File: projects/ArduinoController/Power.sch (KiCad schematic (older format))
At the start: 20 parts

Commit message: working on schematics of Arduino Controller
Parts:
- added U?: ISL21070, symbol ISL21070
- D?: value LED -> V_BAT
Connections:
- net GND: now also U?.3 (GND)
- net VCC_3V3: now also U?.1 (IN)
- new net 2V_Vcc: U?.2 (OUT)
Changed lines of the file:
@@
 	1    0    0    -1
 $EndComp
-Text GLabel 8550 3100 1    47   Output ~ 0
+Text GLabel 8550 3300 1    47   Output ~ 0
 VCC_3V3
 $Comp
@@
 	2700 3800 2700 4250
 Wire Wire Line
-	5000 2750 7900 2750
+	5000 2750 9900 2750
 Connection ~ 5600 2750
 Wire Wire Line
@@
 Wire Wire Line
 	5000 2750 5000 3100
-Text HLabel 7900 2750 2    47   Output ~ 0
+Text HLabel 9900 2750 2    47   Output ~ 0
 5V_Vcc
-Text HLabel 8700 3750 2    47   Output ~ 0
+Text HLabel 9900 3250 2    47   Output ~ 0
 3V3_Vcc
 Connection ~ 7750 2750
@@
 Wire Wire Line
 	7750 3750 7750 2750
-Wire Wire Line
-	8550 3750 8550 3100
 $Comp
 L SWITCH-SPSTPTH2 S?
@@
 P 3250 5250
 F 0 "D?" H 3100 5350 50  0000 C CNN
-F 1 "LED" H 3325 5350 50  0000 C CNN
+F 1 "V_BAT" H 3325 5350 50  0000 C CNN
 F 2 "" H 3250 5250 60  0000 C CNN
 F 3 "" H 3250 5250 60  0000 C CNN
@@
 $EndComp
 Connection ~ 3250 4550
+$Comp
+L ISL21070 U?
+U 1 1 556B667E
+P 9225 3825
+F 0 "U?" H 9225 4125 60  0000 C CNN
+F 1 "ISL21070" H 9225 4025 60  0000 C CNN
+F 2 "" H 9225 3725 60  0000 C CNN
+F 3 "" H 9225 3725 60  0000 C CNN
+	1    9225 3825
+	1    0    0    -1
+$EndComp
+Text HLabel 9900 3750 2    47   Output ~ 0
+2V_Vcc
+$Comp
+L GND #PWR?
+U 1 1 556B66A2
+P 9225 4300
+F 0 "#PWR?" H 9225 4300 30  0001 C CNN
+F 1 "GND" H 9225 4230 30  0001 C CNN
+F 2 "" H 9225 4300 60  0000 C CNN
+F 3 "" H 9225 4300 60  0000 C CNN
+	1    9225 4300
+	1    0    0    -1
+$EndComp
+Wire Wire Line
+	8550 3750 8550 3300
+Wire Wire Line
+	9900 3250 8700 3250
+Wire Wire Line
+	8700 3250 8700 3750
+Wire Wire Line
+	9900 3750 9750 3750
 $EndSCHEMATC

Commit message: work in progress
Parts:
- R?: value R -> 220
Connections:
- net GND: now also S?.1 (O)
- net V_BATT: no longer R?.1
- net Batt_5V: now reaches C?.1, Q?.3 (D), U?.2 (VO)
- net Batt_5V: now also R?.1
- no-connect marks 2 -> 1
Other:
- note added: "Dual OpAmp:\nz.B. LM358\n(SOIC-8)"
- moved on the sheet: D?, R?
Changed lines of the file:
@@
 Wire Wire Line
 	2850 4450 2700 4450
-NoConn ~ 2850 4650
 Wire Wire Line
 	3150 4550 3450 4550
@@
 L R R?
 U 1 1 556AF6F0
-P 3250 4800
-F 0 "R?" V 3330 4800 40  0000 C CNN
-F 1 "R" V 3257 4801 40  0000 C CNN
-F 2 "" V 3180 4800 30  0000 C CNN
-F 3 "" H 3250 4800 30  0000 C CNN
-	1    3250 4800
-	1    0    0    -1
+P 2050 5200
+F 0 "R?" V 2130 5200 40  0000 C CNN
+F 1 "220" V 2057 5201 40  0000 C CNN
+F 2 "" V 1980 5200 30  0000 C CNN
+F 3 "" H 2050 5200 30  0000 C CNN
+	1    2050 5200
+	0    -1   -1   0
 $EndComp
 $Comp
 L LED D?
 U 1 1 556AF704
-P 3250 5250
-F 0 "D?" H 3100 5350 50  0000 C CNN
-F 1 "V_BAT" H 3325 5350 50  0000 C CNN
-F 2 "" H 3250 5250 60  0000 C CNN
-F 3 "" H 3250 5250 60  0000 C CNN
-	1    3250 5250
-	0    1    1    0
+P 2500 5200
+F 0 "D?" H 2350 5300 50  0000 C CNN
+F 1 "V_BAT" H 2575 5300 50  0000 C CNN
+F 2 "" H 2500 5200 60  0000 C CNN
+F 3 "" H 2500 5200 60  0000 C CNN
+	1    2500 5200
+	1    0    0    -1
 $EndComp
 $Comp
 L GND #PWR?
 U 1 1 556AF716
-P 3250 5450
-F 0 "#PWR?" H 3250 5450 30  0001 C CNN
-F 1 "GND" H 3250 5380 30  0001 C CNN
-F 2 "" H 3250 5450 60  0000 C CNN
-F 3 "" H 3250 5450 60  0000 C CNN
-	1    3250 5450
-	1    0    0    -1
+P 2700 5200
+F 0 "#PWR?" H 2700 5200 30  0001 C CNN
+F 1 "GND" H 2700 5130 30  0001 C CNN
+F 2 "" H 2700 5200 60  0000 C CNN
+F 3 "" H 2700 5200 60  0000 C CNN
+	1    2700 5200
+	0    -1   -1   0
 $EndComp
 Connection ~ 3250 4550
@@
 Wire Wire Line
 	9900 3750 9750 3750
+$Comp
+L GND #PWR?
+U 1 1 556CA095
+P 2850 4650
+F 0 "#PWR?" H 2850 4650 30  0001 C CNN
+F 1 "GND" H 2850 4580 30  0001 C CNN
+F 2 "" H 2850 4650 60  0000 C CNN
+F 3 "" H 2850 4650 60  0000 C CNN
+	1    2850 4650
+	0    1    1    0
+$EndComp
+Text GLabel 6300 4200 0    47   Output ~ 0
+Batt_5V
+Wire Wire Line
+	6550 3750 6550 4200
+Wire Wire Line
+	6550 4200 6300 4200
+Text GLabel 1800 5200 0    47   Input ~ 0
+Batt_5V
+Text Notes 4575 4975 0    60   ~ 0
+Dual OpAmp:\nz.B. LM358\n(SOIC-8)
 $EndSCHEMATC

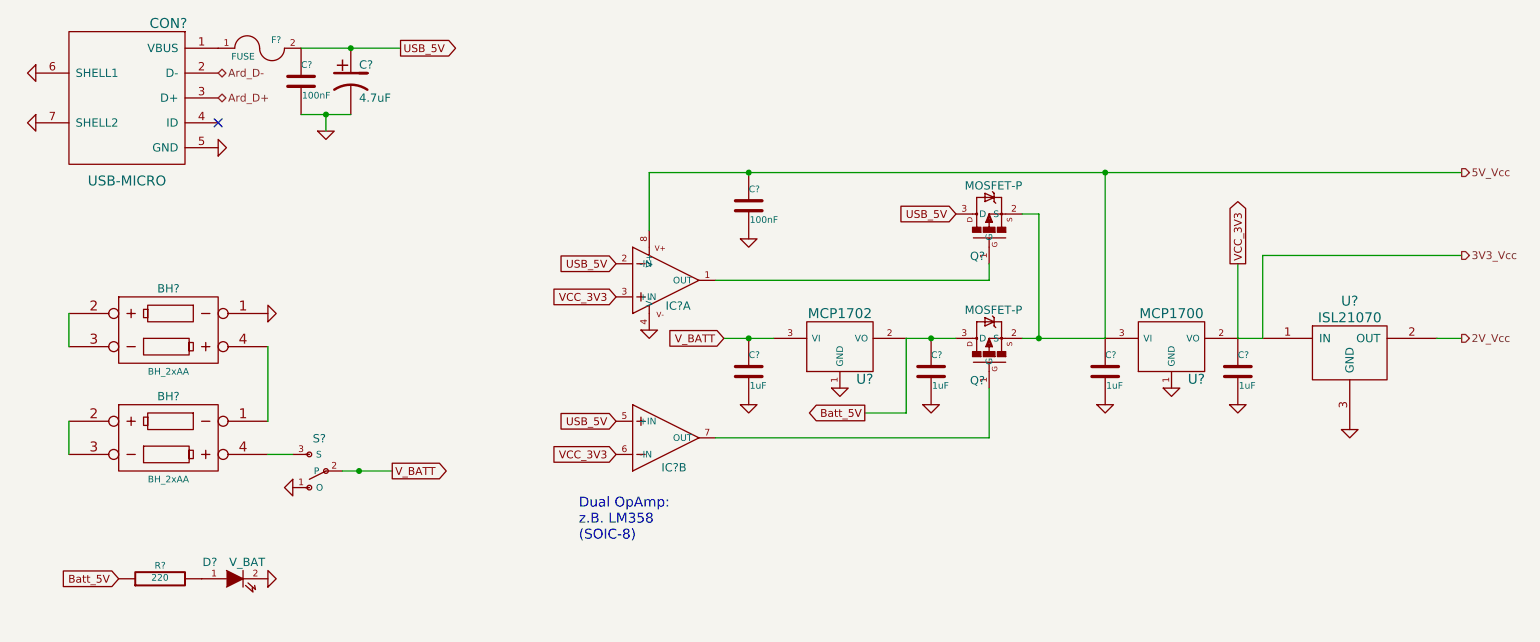
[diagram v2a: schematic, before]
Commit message: schematic passes ERC
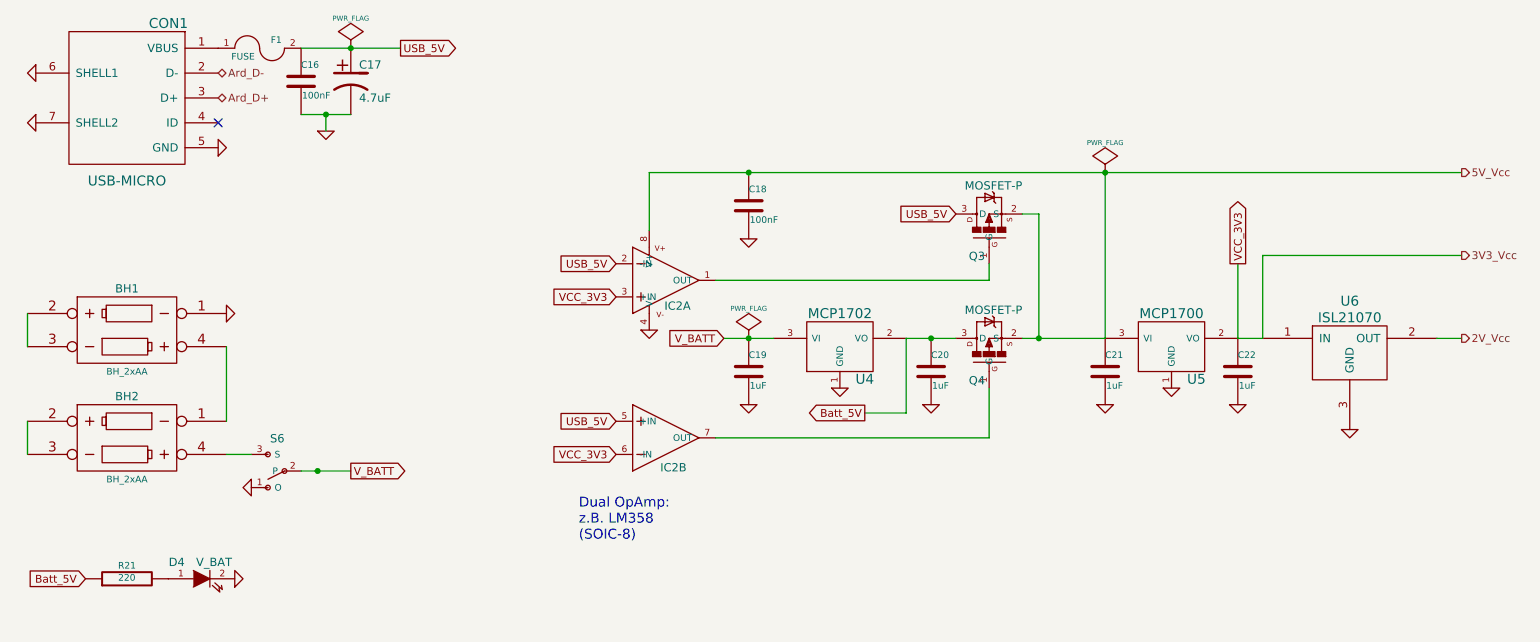
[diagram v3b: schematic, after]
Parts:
- removed BH? (x2): BH_2xAA, symbol BH_2xAA
- removed U?: MCP1702, symbol MCP1702
- removed U?: ISL21070, symbol ISL21070
- added BH1, BH2: BH_2xAA, symbol BH_2xAA
- added U4: MCP1702, symbol MCP1702
- added U6: ISL21070, symbol ISL21070
- gave numbers to parts that had none: 16
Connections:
- net 2V_Vcc: now also U6.2 (OUT)
- net Batt_5V: now also U4.2 (VO)
- net GND: now also BH1.1, U4.1 (GND), U6.3 (GND)
- net VCC_3V3: now also U6.1 (IN)
- net V_BATT: now also U4.3 (VI)
- net at S6.3 (S): now also BH2.4
- new net: BH1.2, BH1.3
- new net: BH1.4, BH2.1
- new net: BH2.2, BH2.3
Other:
- moved on the sheet: D4, R21, S6

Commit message: working on footprints and netlist
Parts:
- removed U4: MCP1702, symbol MCP1702
- added CN1: DCBARREL, DCJACK, symbol DCBARREL
- added U4: NCP1117, symbol NCP1117
- C22: renamed from C19; value 1uF -> 10uF
- C23: renamed from C20; value 1uF -> 10uF
- IC2: value OPAMP-DUALU -> OPAMP-LM358
- renumbered C16 to C19, C17 to C20, C18 to C21, C21 to C24, C22 to C25
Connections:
- net Batt_5V: now also IC2.2 (-IN), IC2.5 (+IN), U4.2 (VO)
- net GND: now also CN1.GND, CN1.GNDB (GNDBREAK), U4.1 (GND); no longer S6.1 (O)
- net USB_5V: no longer IC2.2 (-IN), IC2.5 (+IN)
- net V_BATT: now also U4.3 (VI)
- new net: CN1.PWR, S6.1 (O)
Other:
- note removed: "Dual OpAmp:\nz.B. LM358\n(SOIC-8)"
- moved on the sheet: D4, R21
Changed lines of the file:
@@
 USB_5V
 $Comp
-L GND #PWR053
+L GND #PWR052
 U 1 1 5569964F
 P 2400 2600
-F 0 "#PWR053" H 2400 2600 30  0001 C CNN
+F 0 "#PWR052" H 2400 2600 30  0001 C CNN
 F 1 "GND" H 2400 2530 30  0001 C CNN
 F 2 "" H 2400 2600 60  0000 C CNN
@@
 $EndComp
 $Comp
-L GND #PWR054
+L GND #PWR053
 U 1 1 55699661
 P 1300 2150
-F 0 "#PWR054" H 1300 2150 30  0001 C CNN
+F 0 "#PWR053" H 1300 2150 30  0001 C CNN
 F 1 "GND" H 1300 2080 30  0001 C CNN
 F 2 "" H 1300 2150 60  0000 C CNN
@@
 $EndComp
 $Comp
-L GND #PWR055
+L GND #PWR054
 U 1 1 5569966C
 P 1300 2450
-F 0 "#PWR055" H 1300 2450 30  0001 C CNN
+F 0 "#PWR054" H 1300 2450 30  0001 C CNN
 F 1 "GND" H 1300 2380 30  0001 C CNN
 F 2 "" H 1300 2450 60  0000 C CNN
@@
 $EndComp
 $Comp
-L C C16
+L C C19
 U 1 1 55699766
 P 2900 2200
-F 0 "C16" H 2900 2300 40  0000 L CNN
+F 0 "C19" H 2900 2300 40  0000 L CNN
 F 1 "100nF" H 2906 2115 40  0000 L CNN
 F 2 "" H 2938 2050 30  0000 C CNN
@@
 $EndComp
 $Comp
-L CP1 C17
+L CP1 C20
 U 1 1 5569977A
 P 3200 2200
-F 0 "C17" H 3250 2300 50  0000 L CNN
+F 0 "C20" H 3250 2300 50  0000 L CNN
 F 1 "4.7uF" H 3250 2100 50  0000 L CNN
 F 2 "" H 3200 2200 60  0000 C CNN
@@
 $EndComp
 $Comp
-L GND #PWR056
+L GND #PWR055
 U 1 1 5569978E
 P 3050 2500
-F 0 "#PWR056" H 3050 2500 30  0001 C CNN
+F 0 "#PWR055" H 3050 2500 30  0001 C CNN
 F 1 "GND" H 3050 2430 30  0001 C CNN
 F 2 "" H 3050 2500 60  0000 C CNN
@@
 $EndComp
 $Comp
-L GND #PWR057
+L GND #PWR056
 U 1 1 5569BB18
 P 2450 3600
-F 0 "#PWR057" H 2450 3600 30  0001 C CNN
+F 0 "#PWR056" H 2450 3600 30  0001 C CNN
 F 1 "GND" H 2450 3530 30  0001 C CNN
 F 2 "" H 2450 3600 60  0000 C CNN
@@
 P 5100 4350
 F 0 "IC2" H 5225 4200 50  0000 R TNN
-F 1 "OPAMP-DUALU" H 5300 4550 50  0001 R TNN
+F 1 "OPAMP-LM358" H 5200 4775 50  0000 R TNN
 F 2 "SparkFun-SO08" H 5100 4500 50  0001 C CNN
 F 3 "" H 5100 4350 60  0000 C CNN
@@
 VCC_3V3
 $Comp
-L C C20
+L C C23
 U 1 1 5569F285
 P 6700 3950
-F 0 "C20" H 6700 4050 40  0000 L CNN
-F 1 "1uF" H 6706 3865 40  0000 L CNN
+F 0 "C23" H 6700 4050 40  0000 L CNN
+F 1 "10uF" H 6706 3865 40  0000 L CNN
 F 2 "" H 6738 3800 30  0000 C CNN
 F 3 "" H 6700 3950 60  0000 C CNN
@@
 $EndComp
 $Comp
-L C C19
+L C C22
 U 1 1 5569F290
 P 5600 3950
-F 0 "C19" H 5600 4050 40  0000 L CNN
-F 1 "1uF" H 5606 3865 40  0000 L CNN
+F 0 "C22" H 5600 4050 40  0000 L CNN
+F 1 "10uF" H 5606 3865 40  0000 L CNN
 F 2 "" H 5638 3800 30  0000 C CNN
 F 3 "" H 5600 3950 60  0000 C CNN
@@
 $EndComp
 $Comp
-L GND #PWR058
+L GND #PWR057
 U 1 1 5569F41E
 P 5600 4150
-F 0 "#PWR058" H 5600 4150 30  0001 C CNN
+F 0 "#PWR057" H 5600 4150 30  0001 C CNN
 F 1 "GND" H 5600 4080 30  0001 C CNN
 F 2 "" H 5600 4150 60  0000 C CNN
@@
 $EndComp
 $Comp
-L GND #PWR059
+L GND #PWR058
 U 1 1 5569F429
 P 6700 4150
-F 0 "#PWR059" H 6700 4150 30  0001 C CNN
+F 0 "#PWR058" H 6700 4150 30  0001 C CNN
 F 1 "GND" H 6700 4080 30  0001 C CNN
 F 2 "" H 6700 4150 60  0000 C CNN
@@
 $EndComp
 $Comp
-L GND #PWR060
+L GND #PWR059
 U 1 1 5569F452
 P 6150 4050
-F 0 "#PWR060" H 6150 4050 30  0001 C CNN
+F 0 "#PWR059" H 6150 4050 30  0001 C CNN
 F 1 "GND" H 6150 3980 30  0001 C CNN
 F 2 "" H 6150 4050 60  0000 C CNN
@@
 $EndComp
 $Comp
-L GND #PWR061
+L GND #PWR060
 U 1 1 5569F467
 P 5000 3700
-F 0 "#PWR061" H 5000 3700 30  0001 C CNN
+F 0 "#PWR060" H 5000 3700 30  0001 C CNN
 F 1 "GND" H 5000 3630 30  0001 C CNN
 F 2 "" H 5000 3700 60  0000 C CNN
@@
 $EndComp
 $Comp
-L C C18
+L C C21
 U 1 1 5569F472
 P 5600 2950
-F 0 "C18" H 5600 3050 40  0000 L CNN
+F 0 "C21" H 5600 3050 40  0000 L CNN
 F 1 "100nF" H 5606 2865 40  0000 L CNN
 F 2 "" H 5638 2800 30  0000 C CNN
@@
 $EndComp
 $Comp
-L GND #PWR062
+L GND #PWR061
 U 1 1 5569F482
 P 5600 3150
-F 0 "#PWR062" H 5600 3150 30  0001 C CNN
+F 0 "#PWR061" H 5600 3150 30  0001 C CNN
 F 1 "GND" H 5600 3080 30  0001 C CNN
 F 2 "" H 5600 3150 60  0000 C CNN
@@
 VCC_3V3
 Text GLabel 4800 3300 0    47   Input ~ 0
-USB_5V
+Batt_5V
 Text GLabel 4800 4250 0    47   Input ~ 0
-USB_5V
-$Comp
-L C C21
+Batt_5V
+$Comp
+L C C24
 U 1 1 5569FAC7
 P 7750 3950
-F 0 "C21" H 7750 4050 40  0000 L CNN
+F 0 "C24" H 7750 4050 40  0000 L CNN
 F 1 "1uF" H 7756 3865 40  0000 L CNN
 F 2 "" H 7788 3800 30  0000 C CNN
@@
 $EndComp
 $Comp
-L C C22
+L C C25
 U 1 1 5569FAD2
 P 8550 3950
-F 0 "C22" H 8550 4050 40  0000 L CNN
+F 0 "C25" H 8550 4050 40  0000 L CNN
 F 1 "1uF" H 8556 3865 40  0000 L CNN
 F 2 "" H 8588 3800 30  0000 C CNN
@@
 $EndComp
 $Comp
-L GND #PWR063
+L GND #PWR062
 U 1 1 5569FB9D
 P 7750 4150
-F 0 "#PWR063" H 7750 4150 30  0001 C CNN
+F 0 "#PWR062" H 7750 4150 30  0001 C CNN
 F 1 "GND" H 7750 4080 30  0001 C CNN
 F 2 "" H 7750 4150 60  0000 C CNN
@@
 $EndComp
 $Comp
-L GND #PWR064
+L GND #PWR063
 U 1 1 5569FBA8
 P 8150 4050
-F 0 "#PWR064" H 8150 4050 30  0001 C CNN
+F 0 "#PWR063" H 8150 4050 30  0001 C CNN
 F 1 "GND" H 8150 3980 30  0001 C CNN
 F 2 "" H 8150 4050 60  0000 C CNN
@@
 $EndComp
 $Comp
-L GND #PWR065
+L GND #PWR064
 U 1 1 5569FBB3
 P 8550 4150
-F 0 "#PWR065" H 8550 4150 30  0001 C CNN
+F 0 "#PWR064" H 8550 4150 30  0001 C CNN
 F 1 "GND" H 8550 4080 30  0001 C CNN
 F 2 "" H 8550 4150 60  0000 C CNN
@@
 L R R21
 U 1 1 556AF6F0
-P 1850 5200
-F 0 "R21" V 1930 5200 40  0000 C CNN
-F 1 "220" V 1857 5201 40  0000 C CNN
-F 2 "" V 1780 5200 30  0000 C CNN
-F 3 "" H 1850 5200 30  0000 C CNN
-	1    1850 5200
+P 6400 4900
+F 0 "R21" V 6480 4900 40  0000 C CNN
+F 1 "220" V 6407 4901 40  0000 C CNN
+F 2 "" V 6330 4900 30  0000 C CNN
+F 3 "" H 6400 4900 30  0000 C CNN
+	1    6400 4900
 	0    -1   -1   0
 $EndComp
@@
 L LED D4
 U 1 1 556AF704
-P 2300 5200
-F 0 "D4" H 2150 5300 50  0000 C CNN
-F 1 "V_BAT" H 2375 5300 50  0000 C CNN
-F 2 "" H 2300 5200 60  0000 C CNN
-F 3 "" H 2300 5200 60  0000 C CNN
-	1    2300 5200
-	1    0    0    -1
-$EndComp
-$Comp
-L GND #PWR066
+P 6850 4900
+F 0 "D4" H 6700 5000 50  0000 C CNN
+F 1 "V_BAT" H 6925 5000 50  0000 C CNN
+F 2 "" H 6850 4900 60  0000 C CNN
+F 3 "" H 6850 4900 60  0000 C CNN
+	1    6850 4900
+	1    0    0    -1
+$EndComp
+$Comp
+L GND #PWR065
 U 1 1 556AF716
-P 2500 5200
-F 0 "#PWR066" H 2500 5200 30  0001 C CNN
-F 1 "GND" H 2500 5130 30  0001 C CNN
-F 2 "" H 2500 5200 60  0000 C CNN
-F 3 "" H 2500 5200 60  0000 C CNN
-	1    2500 5200
+P 7050 4900
+F 0 "#PWR065" H 7050 4900 30  0001 C CNN
+F 1 "GND" H 7050 4830 30  0001 C CNN
+F 2 "" H 7050 4900 60  0000 C CNN
+F 3 "" H 7050 4900 60  0000 C CNN
+	1    7050 4900
 	0    -1   -1   0
 $EndComp
@@
 2V_Vcc
 $Comp
-L GND #PWR067
+L GND #PWR066
 U 1 1 556B66A2
 P 9225 4300
-F 0 "#PWR067" H 9225 4300 30  0001 C CNN
+F 0 "#PWR066" H 9225 4300 30  0001 C CNN
 F 1 "GND" H 9225 4230 30  0001 C CNN
 F 2 "" H 9225 4300 60  0000 C CNN
@@
 	9900 3750 9750 3750
 $Comp
-L GND #PWR068
+L GND #PWR067
 U 1 1 556CA095
-P 2600 4650
-F 0 "#PWR068" H 2600 4650 30  0001 C CNN
-F 1 "GND" H 2600 4580 30  0001 C CNN
-F 2 "" H 2600 4650 60  0000 C CNN
-F 3 "" H 2600 4650 60  0000 C CNN
-	1    2600 4650
-	0    1    1    0
+P 2600 5200
+F 0 "#PWR067" H 2600 5200 30  0001 C CNN
+F 1 "GND" H 2600 5130 30  0001 C CNN
+F 2 "" H 2600 5200 60  0000 C CNN
+F 3 "" H 2600 5200 60  0000 C CNN
+	1    2600 5200
+	1    0    0    -1
 $EndComp
 Text GLabel 6300 4200 0    47   Output ~ 0
@@
 Wire Wire Line
 	6550 4200 6300 4200
-Text GLabel 1600 5200 0    47   Input ~ 0
+Text GLabel 6150 4900 0    47   Input ~ 0
 Batt_5V
-Text Notes 4575 4975 0    60   ~ 0
-Dual OpAmp:\nz.B. LM358\n(SOIC-8)
-$Comp
-L MCP1702 U4
-U 1 1 556E9FC1
-P 6150 3800
-F 0 "U4" H 6300 3604 60  0000 C CNN
-F 1 "MCP1702" H 6150 4000 60  0000 C CNN
-F 2 "" H 6150 3800 60  0000 C CNN
-F 3 "" H 6150 3800 60  0000 C CNN
-	1    6150 3800
-	1    0    0    -1
-$EndComp
 $Comp
 L BH_2xAA BH1
@@
 $EndComp
 $Comp
-L PWR_FLAG #FLG069
+L PWR_FLAG #FLG068
 U 1 1 557177D7
 P 5600 3750
-F 0 "#FLG069" H 5600 3845 30  0001 C CNN
+F 0 "#FLG068" H 5600 3845 30  0001 C CNN
 F 1 "PWR_FLAG" H 5600 3930 30  0000 C CNN
 F 2 "" H 5600 3750 60  0000 C CNN
@@
 $EndComp
 $Comp
-L PWR_FLAG #FLG070
+L PWR_FLAG #FLG069
 U 1 1 55718314
 P 3200 2000
-F 0 "#FLG070" H 3200 2095 30  0001 C CNN
+F 0 "#FLG069" H 3200 2095 30  0001 C CNN
 F 1 "PWR_FLAG" H 3200 2180 30  0000 C CNN
 F 2 "" H 3200 2000 60  0000 C CNN
@@
 $EndComp
 $Comp
-L PWR_FLAG #FLG071
+L PWR_FLAG #FLG070
 U 1 1 557185B0
 P 7750 2750
-F 0 "#FLG071" H 7750 2845 30  0001 C CNN
+F 0 "#FLG070" H 7750 2845 30  0001 C CNN
 F 1 "PWR_FLAG" H 7750 2930 30  0000 C CNN
 F 2 "" H 7750 2750 60  0000 C CNN
@@
 	1    0    0    -1
 $EndComp
+$Comp
+L NCP1117 U4
+U 1 1 5575DD78
+P 6150 3800
+F 0 "U4" H 6300 3604 60  0000 C CNN
+F 1 "NCP1117" H 6150 4000 60  0000 C CNN
+F 2 "" H 6150 3800 60  0000 C CNN
+F 3 "" H 6150 3800 60  0000 C CNN
+	1    6150 3800
+	1    0    0    -1
+$EndComp
+$Comp
+L DCBARREL CN1
+U 1 1 5575E1C3
+P 2050 5000
+F 0 "CN1" H 1850 5150 50  0000 L BNN
+F 1 "DCBARREL" H 1850 4800 50  0000 L BNN
+F 2 "DCJACK" H 2050 5150 50  0001 C CNN
+F 3 "" H 2050 5000 60  0000 C CNN
+	1    2050 5000
+	1    0    0    -1
+$EndComp
+Wire Wire Line
+	2150 4900 2600 4900
+Wire Wire Line
+	2600 4900 2600 4650
+Wire Wire Line
+	2150 5000 2150 5100
+Wire Wire Line
+	2150 5100 2600 5100
+Wire Wire Line
+	2600 5100 2600 5200
+$Comp
+L PWR_FLAG #FLG071
+U 1 1 5575E56D
+P 2150 4900
+F 0 "#FLG071" H 2150 4995 30  0001 C CNN
+F 1 "PWR_FLAG" H 2150 5080 30  0000 C CNN
+F 2 "" H 2150 4900 60  0000 C CNN
+F 3 "" H 2150 4900 60  0000 C CNN
+	1    2150 4900
+	1    0    0    -1
+$EndComp

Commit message: more footprints added
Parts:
- removed CON1: USB-MICRO, symbol USB-MINI-B-Vert
- added CON1: USB-MICRO, symbol USB-MICRO
- renumbered IC2 to IC3
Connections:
- net Ard_D+: now also CON1.3 (D+)
- net Ard_D-: now also CON1.2 (D-)
- net GND: now also CON1.5 (GND), CON1.6 (SHELL1), CON1.7 (SHELL2), CON1.8 (SHELL3), CON1.9 (SHELL4)
- net at F1.1: now also CON1.1 (VBUS)
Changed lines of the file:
@@
 Comment4 "Arduino Esplora clone"
 $EndDescr
-$Comp
-L USB-MINI-B-Vert CON1
-U 1 1 55699629
-P 1850 2300
-F 0 "CON1" H 1600 2750 60  0000 C CNN
-F 1 "USB-MICRO" H 1850 1800 60  0000 C CNN
-F 2 "" H 1850 2300 60  0000 C CNN
-F 3 "" H 1850 2300 60  0000 C CNN
-	1    1850 2300
-	-1   0    0    -1
-$EndComp
 Text GLabel 3500 2000 2    47   Output ~ 0
 USB_5V
@@
 $EndComp
 $Comp
-L OPAMP-DUALU IC2
+L OPAMP-DUALU IC3
 U 2 1 5569D3B3
 P 5100 4350
-F 0 "IC2" H 5225 4200 50  0000 R TNN
+F 0 "IC3" H 5225 4200 50  0000 R TNN
 F 1 "OPAMP-LM358" H 5200 4775 50  0000 R TNN
 F 2 "SparkFun-SO08" H 5100 4500 50  0001 C CNN
@@
 	1    0    0    -1
 $EndComp
+$Comp
+L USB-MICRO CON1
+U 1 1 5577520F
+P 1850 2300
+F 0 "CON1" H 1600 2750 60  0000 C CNN
+F 1 "USB-MICRO" H 1800 1800 60  0000 C CNN
+F 2 "" H 1850 2300 60  0000 C CNN
+F 3 "" H 1850 2300 60  0000 C CNN
+	1    1850 2300
+	-1   0    0    -1
+$EndComp
+$Comp
+L GND #PWR072
+U 1 1 5577523E
+P 1300 2000
+F 0 "#PWR072" H 1300 2000 30  0001 C CNN
+F 1 "GND" H 1300 1930 30  0001 C CNN
+F 2 "" H 1300 2000 60  0000 C CNN
+F 3 "" H 1300 2000 60  0000 C CNN
+	1    1300 2000
+	0    1    1    0
+$EndComp
+$Comp
+L GND #PWR073
+U 1 1 55775249
+P 1300 2600
+F 0 "#PWR073" H 1300 2600 30  0001 C CNN
+F 1 "GND" H 1300 2530 30  0001 C CNN
+F 2 "" H 1300 2600 60  0000 C CNN
+F 3 "" H 1300 2600 60  0000 C CNN
+	1    1300 2600
+	0    1    1    0
+$EndComp
 $EndSCHEMATC

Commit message: footprints done
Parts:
- removed IC3: OPAMP-LM358, SparkFun-SO08, symbol OPAMP-DUALU
- removed S6: SWITCH-SPSTPTH2, switch, symbol SWITCH-SPSTPTH2
- added unit 2 of IC2
- added S6: SPDT, symbol SPDT
- IC2: value OPAMP-DUALU -> LM358
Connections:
- net Batt_5V: now also IC2.3 (+IN), IC2.6 (-IN); no longer IC2.2 (-IN)
- net GND: now also S6.4 (Shield), S6.5 (Shield)
- net VCC_3V3: now also IC2.2 (-IN), IC2.5 (+IN); no longer IC2.3 (+IN)
- net V_BATT: now also S6.2 (C)
- net at Q4.1 (G): now also IC2.7 (OUT)
- net at CN1.PWR: now also S6.3 (B)
- net at BH2.4: now also S6.1 (A)
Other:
- moved on the sheet: C21, C22, C23, C24, C25, Q3, Q4, U4, U5, U6
